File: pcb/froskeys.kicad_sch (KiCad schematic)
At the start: 30 parts, among them J1 OLED, SW1 MX, SW10 RotaryEncoder_Switch, SW2 MX, SW3 MX, SW4 MX, SW5 MX, SW6 MX, SW7 MX, SW8 MX, SW9 MX, U1 XIAO-RP2040-DIP

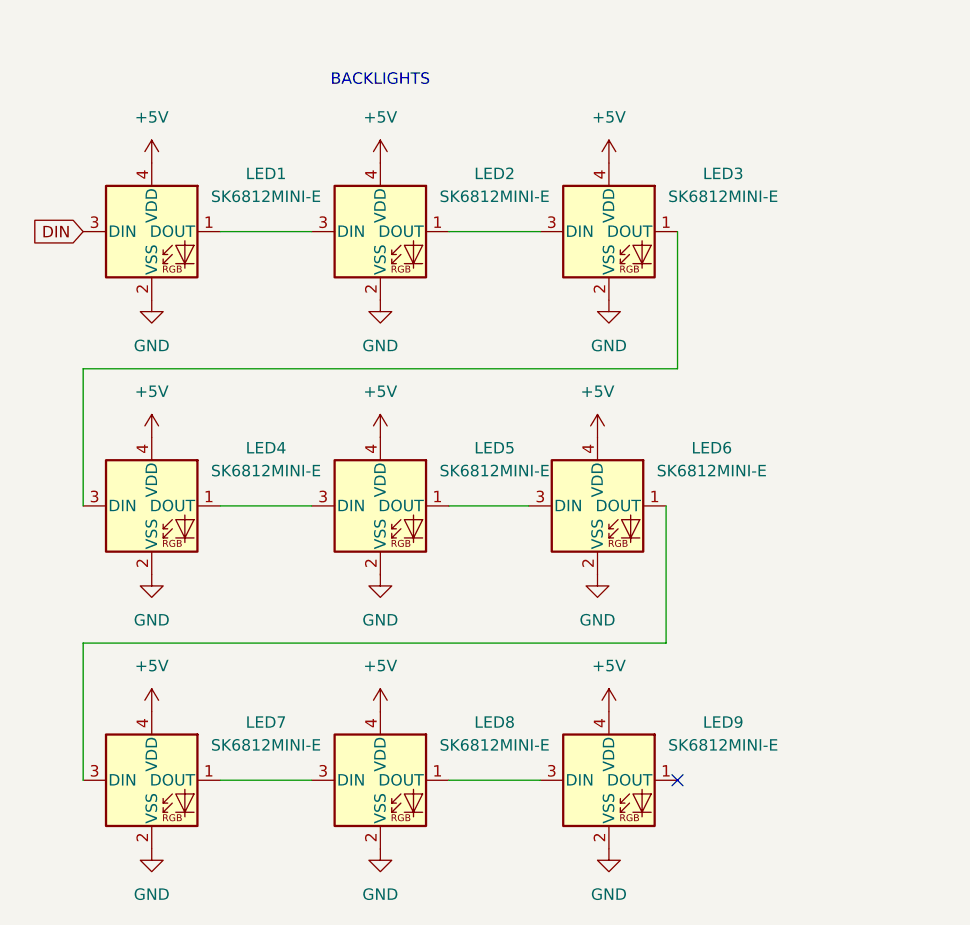
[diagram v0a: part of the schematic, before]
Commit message: Change SK6812 pin order
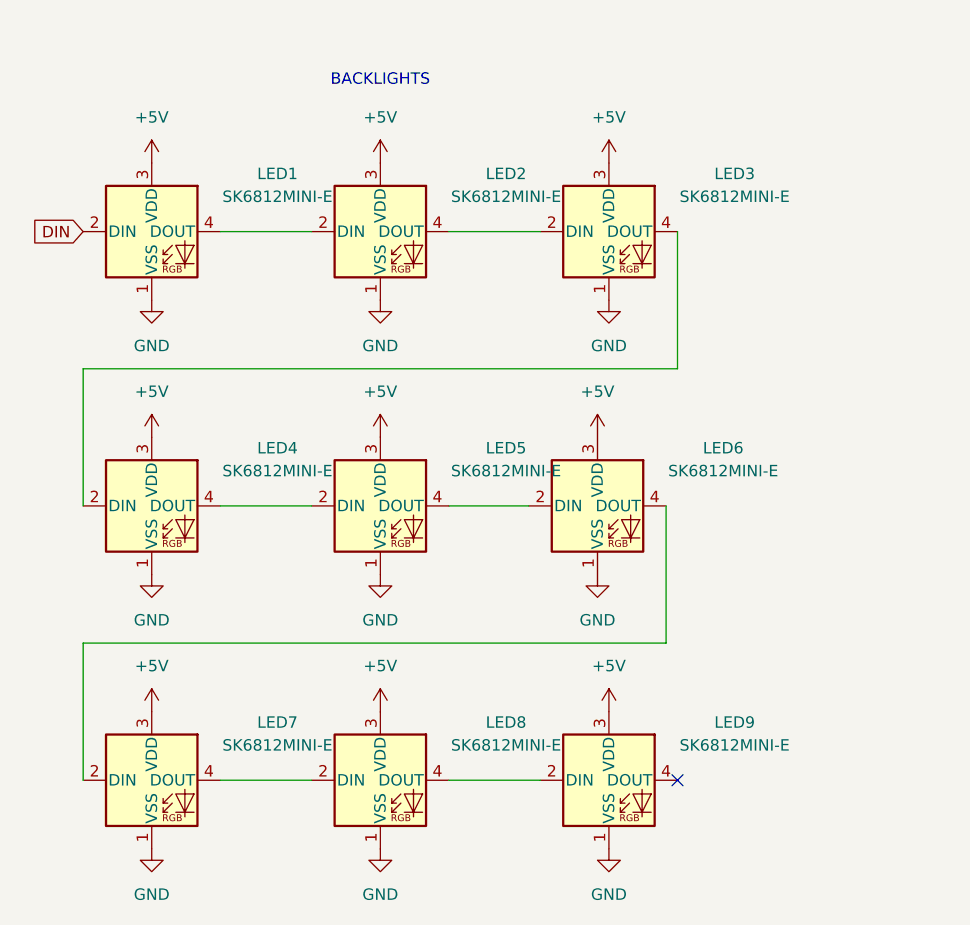
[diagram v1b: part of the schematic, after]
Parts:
- LED1, LED2, LED3, LED4, LED5, LED6, LED7, LED8, LED9: footprint Keyboard Parts:MX_SK6812MINI-E -> Keyboard Parts:MX_SK6812MINI-E_GOOD; symbol LED:SK6812MINI -> LED:SK6812
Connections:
- net +5V: now also LED1.3 (VDD), LED2.3 (VDD), LED3.3 (VDD), LED4.3 (VDD), LED5.3 (VDD), LED6.3 (VDD), LED7.3 (VDD), LED8.3 (VDD), LED9.3 (VDD); no longer LED1.4 (VDD), LED2.4 (VDD), LED3.4 (VDD), LED4.4 (VDD), LED5.4 (VDD), LED6.4 (VDD), LED7.4 (VDD), LED8.4 (VDD), LED9.4 (VDD)
- net DIN: now also LED1.2 (DIN); no longer LED1.3 (DIN)
- net GND: now also LED1.1 (VSS), LED2.1 (VSS), LED3.1 (VSS), LED4.1 (VSS), LED5.1 (VSS), LED6.1 (VSS), LED7.1 (VSS), LED8.1 (VSS), LED9.1 (VSS); no longer LED1.2 (VSS), LED2.2 (VSS), LED3.2 (VSS), LED4.2 (VSS), LED5.2 (VSS), LED6.2 (VSS), LED7.2 (VSS), LED8.2 (VSS), LED9.2 (VSS)
- new net: LED5.4 (DOUT), LED6.2 (DIN)
- new net: LED6.4 (DOUT), LED7.2 (DIN)
- new net: LED1.4 (DOUT), LED2.2 (DIN)
- new net: LED2.4 (DOUT), LED3.2 (DIN)
- new net: LED3.4 (DOUT), LED4.2 (DIN)
- new net: LED4.4 (DOUT), LED5.2 (DIN)
- new net: LED7.4 (DOUT), LED8.2 (DIN)
- new net: LED8.4 (DOUT), LED9.2 (DIN)
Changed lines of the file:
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@@
 	(title_block
 		(title "Froskeys")
-		(date "2025-06-22")
-		(rev "1")
+		(date "2025-09-27")
+		(rev "2")
 		(company "Frosetrain")
 	)
@@
 	)
 	(symbol
-		(lib_id "LED:SK6812MINI")
+		(lib_id "LED:SK6812")
 		(at 105.41 124.46 0)
 		(unit 1)
@@
 		(fields_autoplaced yes)
 		(property "Reference" "LED6"
-			(at 118.11 118.0398 0)
+			(at 119.38 118.0398 0)
 			(effects
 				(font
@@
 		)
 		(property "Value" "SK6812MINI-E"
-			(at 118.11 120.5798 0)
+			(at 119.38 120.5798 0)
 			(effects
 				(font
@@
 			)
 		)
-		(property "Footprint" "Keyboard Parts:MX_SK6812MINI-E"
+		(property "Footprint" "Keyboard Parts:MX_SK6812MINI-E_GOOD"
 			(at 106.68 132.08 0)
 			(effects
@@
 			)
 		)
-		(property "Datasheet" "https://cdn-shop.adafruit.com/product-files/2686/SK6812MINI_REV.01-1-2.pdf"
+		(property "Datasheet" "https://cdn-shop.adafruit.com/product-files/1138/SK6812+LED+datasheet+.pdf"
 			(at 107.95 133.985 0)
 			(effects
@@
 	)
 	(symbol
-		(lib_id "LED:SK6812MINI")
+		(lib_id "LED:SK6812")
 		(at 55.88 93.98 0)
 		(unit 1)
@@
 		(fields_autoplaced yes)
 		(property "Reference" "LED1"
-			(at 68.58 87.5598 0)
+			(at 69.85 87.5598 0)
 			(effects
 				(font
@@
 		)
 		(property "Value" "SK6812MINI-E"
-			(at 68.58 90.0998 0)
+			(at 69.85 90.0998 0)
 			(effects
 				(font
@@
 			)
 		)
-		(property "Footprint" "Keyboard Parts:MX_SK6812MINI-E"
+		(property "Footprint" "Keyboard Parts:MX_SK6812MINI-E_GOOD"
 			(at 57.15 101.6 0)
 			(effects
@@
 			)
 		)
-		(property "Datasheet" "https://cdn-shop.adafruit.com/product-files/2686/SK6812MINI_REV.01-1-2.pdf"
+		(property "Datasheet" "https://cdn-shop.adafruit.com/product-files/1138/SK6812+LED+datasheet+.pdf"
 			(at 58.42 103.505 0)
 			(effects
@@
 	)
 	(symbol
-		(lib_id "LED:SK6812MINI")
+		(lib_id "LED:SK6812")
 		(at 106.68 93.98 0)
 		(unit 1)
@@
 		(fields_autoplaced yes)
 		(property "Reference" "LED3"
-			(at 119.38 87.5598 0)
+			(at 120.65 87.5598 0)
 			(effects
 				(font
@@
 		)
 		(property "Value" "SK6812MINI-E"
-			(at 119.38 90.0998 0)
+			(at 120.65 90.0998 0)
 			(effects
 				(font
@@
 			)
 		)
-		(property "Footprint" "Keyboard Parts:MX_SK6812MINI-E"
+		(property "Footprint" "Keyboard Parts:MX_SK6812MINI-E_GOOD"
 			(at 107.95 101.6 0)
 			(effects
@@
 			)
 		)
-		(property "Datasheet" "https://cdn-shop.adafruit.com/product-files/2686/SK6812MINI_REV.01-1-2.pdf"
+		(property "Datasheet" "https://cdn-shop.adafruit.com/product-files/1138/SK6812+LED+datasheet+.pdf"
 			(at 109.22 103.505 0)
 			(effects
@@
 	)
 	(symbol
-		(lib_id "LED:SK6812MINI")
+		(lib_id "LED:SK6812")
 		(at 81.28 124.46 0)
 		(unit 1)
@@
 		(fields_autoplaced yes)
 		(property "Reference" "LED5"
-			(at 93.98 118.0398 0)
+			(at 95.25 118.0398 0)
 			(effects
 				(font
@@
 		)
 		(property "Value" "SK6812MINI-E"
-			(at 93.98 120.5798 0)
+			(at 95.25 120.5798 0)
 			(effects
 				(font
@@
 			)
 		)
-		(property "Footprint" "Keyboard Parts:MX_SK6812MINI-E"
+		(property "Footprint" "Keyboard Parts:MX_SK6812MINI-E_GOOD"
 			(at 82.55 132.08 0)
 			(effects
@@
 			)
 		)
-		(property "Datasheet" "https://cdn-shop.adafruit.com/product-files/2686/SK6812MINI_REV.01-1-2.pdf"
+		(property "Datasheet" "https://cdn-shop.adafruit.com/product-files/1138/SK6812+LED+datasheet+.pdf"
 			(at 83.82 133.985 0)
 			(effects
@@
 	)
 	(symbol
-		(lib_id "LED:SK6812MINI")
+		(lib_id "LED:SK6812")
 		(at 55.88 154.94 0)
 		(unit 1)
@@
 		(fields_autoplaced yes)
 		(property "Reference" "LED7"
-			(at 68.58 148.5198 0)
+			(at 69.85 148.5198 0)
 			(effects
 				(font
@@
 		)
 		(property "Value" "SK6812MINI-E"
-			(at 68.58 151.0598 0)
+			(at 69.85 151.0598 0)
 			(effects
 				(font
@@
 			)
 		)
-		(property "Footprint" "Keyboard Parts:MX_SK6812MINI-E"
+		(property "Footprint" "Keyboard Parts:MX_SK6812MINI-E_GOOD"
 			(at 57.15 162.56 0)
 			(effects
@@
 			)
 		)
-		(property "Datasheet" "https://cdn-shop.adafruit.com/product-files/2686/SK6812MINI_REV.01-1-2.pdf"
+		(property "Datasheet" "https://cdn-shop.adafruit.com/product-files/1138/SK6812+LED+datasheet+.pdf"
 			(at 58.42 164.465 0)
 			(effects
@@
 	)
 	(symbol
-		(lib_id "LED:SK6812MINI")
+		(lib_id "LED:SK6812")
 		(at 81.28 154.94 0)
 		(unit 1)
@@
 		(fields_autoplaced yes)
 		(property "Reference" "LED8"
-			(at 93.98 148.5198 0)
+			(at 95.25 148.5198 0)
 			(effects
 				(font
@@
 		)
 		(property "Value" "SK6812MINI-E"
-			(at 93.98 151.0598 0)
+			(at 95.25 151.0598 0)
 			(effects
 				(font
@@
 			)
 		)
-		(property "Footprint" "Keyboard Parts:MX_SK6812MINI-E"
+		(property "Footprint" "Keyboard Parts:MX_SK6812MINI-E_GOOD"
 			(at 82.55 162.56 0)
 			(effects
@@
 			)
 		)
-		(property "Datasheet" "https://cdn-shop.adafruit.com/product-files/2686/SK6812MINI_REV.01-1-2.pdf"
+		(property "Datasheet" "https://cdn-shop.adafruit.com/product-files/1138/SK6812+LED+datasheet+.pdf"
 			(at 83.82 164.465 0)
 			(effects
@@
 	)
 	(symbol
-		(lib_id "LED:SK6812MINI")
+		(lib_id "LED:SK6812")
 		(at 106.68 154.94 0)
 		(unit 1)
@@
 		(fields_autoplaced yes)
 		(property "Reference" "LED9"
-			(at 119.38 148.5198 0)
+			(at 120.65 148.5198 0)
 			(effects
 				(font
@@
 		)
 		(property "Value" "SK6812MINI-E"
-			(at 119.38 151.0598 0)
+			(at 120.65 151.0598 0)
 			(effects
 				(font
@@
 			)
 		)
-		(property "Footprint" "Keyboard Parts:MX_SK6812MINI-E"
+		(property "Footprint" "Keyboard Parts:MX_SK6812MINI-E_GOOD"
 			(at 107.95 162.56 0)
 			(effects
@@
 			)
 		)
-		(property "Datasheet" "https://cdn-shop.adafruit.com/product-files/2686/SK6812MINI_REV.01-1-2.pdf"
+		(property "Datasheet" "https://cdn-shop.adafruit.com/product-files/1138/SK6812+LED+datasheet+.pdf"
 			(at 109.22 164.465 0)
 			(effects
@@
 	)
 	(symbol
-		(lib_id "LED:SK6812MINI")
+		(lib_id "LED:SK6812")
 		(at 55.88 124.46 0)
 		(unit 1)
@@
 		(fields_autoplaced yes)
 		(property "Reference" "LED4"
-			(at 68.58 118.0398 0)
+			(at 69.85 118.0398 0)
 			(effects
 				(font
@@
 		)
 		(property "Value" "SK6812MINI-E"
-			(at 68.58 120.5798 0)
+			(at 69.85 120.5798 0)
 			(effects
 				(font
@@
 			)
 		)
-		(property "Footprint" "Keyboard Parts:MX_SK6812MINI-E"
+		(property "Footprint" "Keyboard Parts:MX_SK6812MINI-E_GOOD"
 			(at 57.15 132.08 0)
 			(effects
@@
 			)
 		)
-		(property "Datasheet" "https://cdn-shop.adafruit.com/product-files/2686/SK6812MINI_REV.01-1-2.pdf"
+		(property "Datasheet" "https://cdn-shop.adafruit.com/product-files/1138/SK6812+LED+datasheet+.pdf"
 			(at 58.42 133.985 0)
 			(effects
@@
 	)
 	(symbol
-		(lib_id "LED:SK6812MINI")
+		(lib_id "LED:SK6812")
 		(at 81.28 93.98 0)
 		(unit 1)
@@
 		(fields_autoplaced yes)
 		(property "Reference" "LED2"
-			(at 93.98 87.5598 0)
+			(at 95.25 87.5598 0)
 			(effects
 				(font
@@
 		)
 		(property "Value" "SK6812MINI-E"
-			(at 93.98 90.0998 0)
+			(at 95.25 90.0998 0)
 			(effects
 				(font
@@
 			)
 		)
-		(property "Footprint" "Keyboard Parts:MX_SK6812MINI-E"
+		(property "Footprint" "Keyboard Parts:MX_SK6812MINI-E_GOOD"
 			(at 82.55 101.6 0)
 			(effects
@@
 			)
 		)
-		(property "Datasheet" "https://cdn-shop.adafruit.com/product-files/2686/SK6812MINI_REV.01-1-2.pdf"
+		(property "Datasheet" "https://cdn-shop.adafruit.com/product-files/1138/SK6812+LED+datasheet+.pdf"
 			(at 83.82 103.505 0)
 			(effects
